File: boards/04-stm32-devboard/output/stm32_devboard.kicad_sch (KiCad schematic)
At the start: 17 parts, among them J1 SWD-6, U1 AMS1117-3.3, U2 STM32F103C8T6, Y1 8MHz

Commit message: chore(boards): regenerate schematics after crystal-factory refactor
Regenerates board 03/04/05 schematics from their refactored generator
scripts after rebase onto current main (post-merge of #2575/#2577/#2576).
Diff for board 03 shows two new C symbols (C5, C6 - the
previously-missing 22pF load caps); diffs for boards 04 and 05 are
mostly UUID changes since the refactor produces equivalent layouts.

Refs #2568.

Co-Authored-By: Claude Opus 4.7 (1M context) <noreply@anthropic.com>
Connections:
- net +5V: now also R2.1; no longer R2.2
- net at U2.26 (PB13): now also R2.2; no longer R2.1
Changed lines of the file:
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@@
 		(instances
 			(project "project"
-				(path "/44e716c7-27f0-4b1c-9394-2988dc26182d" (reference "U1") (unit 1)
+				(path "/d46a8a86-8bb3-4cd7-bb33-5e0ed20b6923" (reference "U1") (unit 1)
 				)
 			)
@@
 		(instances
 			(project "project"
-				(path "/44e716c7-27f0-4b1c-9394-2988dc26182d" (reference "C1") (unit 1)
+				(path "/d46a8a86-8bb3-4cd7-bb33-5e0ed20b6923" (reference "C1") (unit 1)
 				)
 			)
@@
 		(instances
 			(project "project"
-				(path "/44e716c7-27f0-4b1c-9394-2988dc26182d" (reference "C2") (unit 1)
+				(path "/d46a8a86-8bb3-4cd7-bb33-5e0ed20b6923" (reference "C2") (unit 1)
 				)
 			)
@@
 		(instances
 			(project "project"
-				(path "/44e716c7-27f0-4b1c-9394-2988dc26182d" (reference "C3") (unit 1)
+				(path "/d46a8a86-8bb3-4cd7-bb33-5e0ed20b6923" (reference "C3") (unit 1)
 				)
 			)
@@
 		(instances
 			(project "project"
-				(path "/44e716c7-27f0-4b1c-9394-2988dc26182d" (reference "U2") (unit 1)
+				(path "/d46a8a86-8bb3-4cd7-bb33-5e0ed20b6923" (reference "U2") (unit 1)
 				)
 			)
@@
 		(instances
 			(project "project"
-				(path "/44e716c7-27f0-4b1c-9394-2988dc26182d" (reference "C12") (unit 1)
+				(path "/d46a8a86-8bb3-4cd7-bb33-5e0ed20b6923" (reference "C12") (unit 1)
 				)
 			)
@@
 		(instances
 			(project "project"
-				(path "/44e716c7-27f0-4b1c-9394-2988dc26182d" (reference "C13") (unit 1)
+				(path "/d46a8a86-8bb3-4cd7-bb33-5e0ed20b6923" (reference "C13") (unit 1)
 				)
 			)
@@
 		(instances
 			(project "project"
-				(path "/44e716c7-27f0-4b1c-9394-2988dc26182d" (reference "C14") (unit 1)
+				(path "/d46a8a86-8bb3-4cd7-bb33-5e0ed20b6923" (reference "C14") (unit 1)
 				)
 			)
@@
 		(instances
 			(project "project"
-				(path "/44e716c7-27f0-4b1c-9394-2988dc26182d" (reference "C15") (unit 1)
+				(path "/d46a8a86-8bb3-4cd7-bb33-5e0ed20b6923" (reference "C15") (unit 1)
 				)
 			)
@@
 		(instances
 			(project "project"
-				(path "/44e716c7-27f0-4b1c-9394-2988dc26182d" (reference "C16") (unit 1)
+				(path "/d46a8a86-8bb3-4cd7-bb33-5e0ed20b6923" (reference "C16") (unit 1)
 				)
 			)
@@
 		(instances
 			(project "project"
-				(path "/44e716c7-27f0-4b1c-9394-2988dc26182d" (reference "Y1") (unit 1)
+				(path "/d46a8a86-8bb3-4cd7-bb33-5e0ed20b6923" (reference "Y1") (unit 1)
 				)
 			)
@@
 		(instances
 			(project "project"
-				(path "/44e716c7-27f0-4b1c-9394-2988dc26182d" (reference "C10") (unit 1)
+				(path "/d46a8a86-8bb3-4cd7-bb33-5e0ed20b6923" (reference "C10") (unit 1)
 				)
 			)
@@
 		(instances
 			(project "project"
-				(path "/44e716c7-27f0-4b1c-9394-2988dc26182d" (reference "C11") (unit 1)
+				(path "/d46a8a86-8bb3-4cd7-bb33-5e0ed20b6923" (reference "C11") (unit 1)
 				)
 			)
@@
 		(instances
 			(project "project"
-				(path "/44e716c7-27f0-4b1c-9394-2988dc26182d" (reference "J1") (unit 1)
+				(path "/d46a8a86-8bb3-4cd7-bb33-5e0ed20b6923" (reference "J1") (unit 1)
 				)
 			)
@@
 	(symbol
 		(lib_id "Device:R")
-		(at 171.45 147.32 270)
+		(at 171.45 152.4 0)
 		(unit 1)
 		(exclude_from_sim no)
@@
 		(dnp no)
 		(property "Reference" "R2"
-			(at 171.45 142.24 0)
+			(at 171.45 147.32 0)
 			(effects
 				(font
@@
 		)
 		(property "Value" "10k"
-			(at 171.45 144.78 0)
+			(at 171.45 149.86 0)
 			(effects
 				(font
@@
 		)
 		(property "Footprint" "Resistor_SMD:R_0805_2012Metric"
-			(at 171.45 147.32 0)
+			(at 171.45 152.4 0)
 			(effects
 				(font
@@
 		)
 		(property "Datasheet" "~"
-			(at 171.45 147.32 0)
+			(at 171.45 152.4 0)
 			(effects
 				(font
@@
 		(instances
 			(project "project"
-				(path "/44e716c7-27f0-4b1c-9394-2988dc26182d" (reference "R2") (unit 1)
+				(path "/d46a8a86-8bb3-4cd7-bb33-5e0ed20b6923" (reference "R2") (unit 1)
 				)
 			)
@@
 		(instances
 			(project "project"
-				(path "/44e716c7-27f0-4b1c-9394-2988dc26182d" (reference "D1") (unit 1)
+				(path "/d46a8a86-8bb3-4cd7-bb33-5e0ed20b6923" (reference "D1") (unit 1)
 				)
 			)
@@
 		(instances
 			(project "project"
-				(path "/44e716c7-27f0-4b1c-9394-2988dc26182d" (reference "R1") (unit 1)
+				(path "/d46a8a86-8bb3-4cd7-bb33-5e0ed20b6923" (reference "R1") (unit 1)
 				)
 			)
@@
 		(instances
 			(project "project"
-				(path "/44e716c7-27f0-4b1c-9394-2988dc26182d" (reference "#PWR01") (unit 1)
+				(path "/d46a8a86-8bb3-4cd7-bb33-5e0ed20b6923" (reference "#PWR01") (unit 1)
 				)
 			)
@@
 		(instances
 			(project "project"
-				(path "/44e716c7-27f0-4b1c-9394-2988dc26182d" (reference "#PWR02") (unit 1)
+				(path "/d46a8a86-8bb3-4cd7-bb33-5e0ed20b6923" (reference "#PWR02") (unit 1)
 				)
 			)
@@
 		(instances
 			(project "project"
-				(path "/44e716c7-27f0-4b1c-9394-2988dc26182d" (reference "#PWR03") (unit 1)
+				(path "/d46a8a86-8bb3-4cd7-bb33-5e0ed20b6923" (reference "#PWR03") (unit 1)
 				)
 			)
@@
 	)
 	(wire
-		(pts (xy 191.77 147.32) (xy 175.26 147.32))
-		(stroke
-			(width 0)
-			(type default)
-		)
-	)
-	(wire
-		(pts (xy 167.64 147.32) (xy 167.64 199.39))
+		(pts (xy 191.77 147.32) (xy 171.45 156.21))
+		(stroke
+			(width 0)
+			(type default)
+		)
+	)
+	(wire
+		(pts (xy 171.45 148.59) (xy 171.45 199.39))
 		(stroke
 			(width 0)
@@
 	)
 	(junction
-		(at 167.64 199.39)
+		(at 171.45 199.39)
 		(diameter 0)
 	)
@@
 	)
 	(sheet_instances
-		(path "/44e716c7-27f0-4b1c-9394-2988dc26182d" (page 1)
-		)
-	)
+		(path "/d46a8a86-8bb3-4cd7-bb33-5e0ed20b6923" (page 1)
+		)
+	)

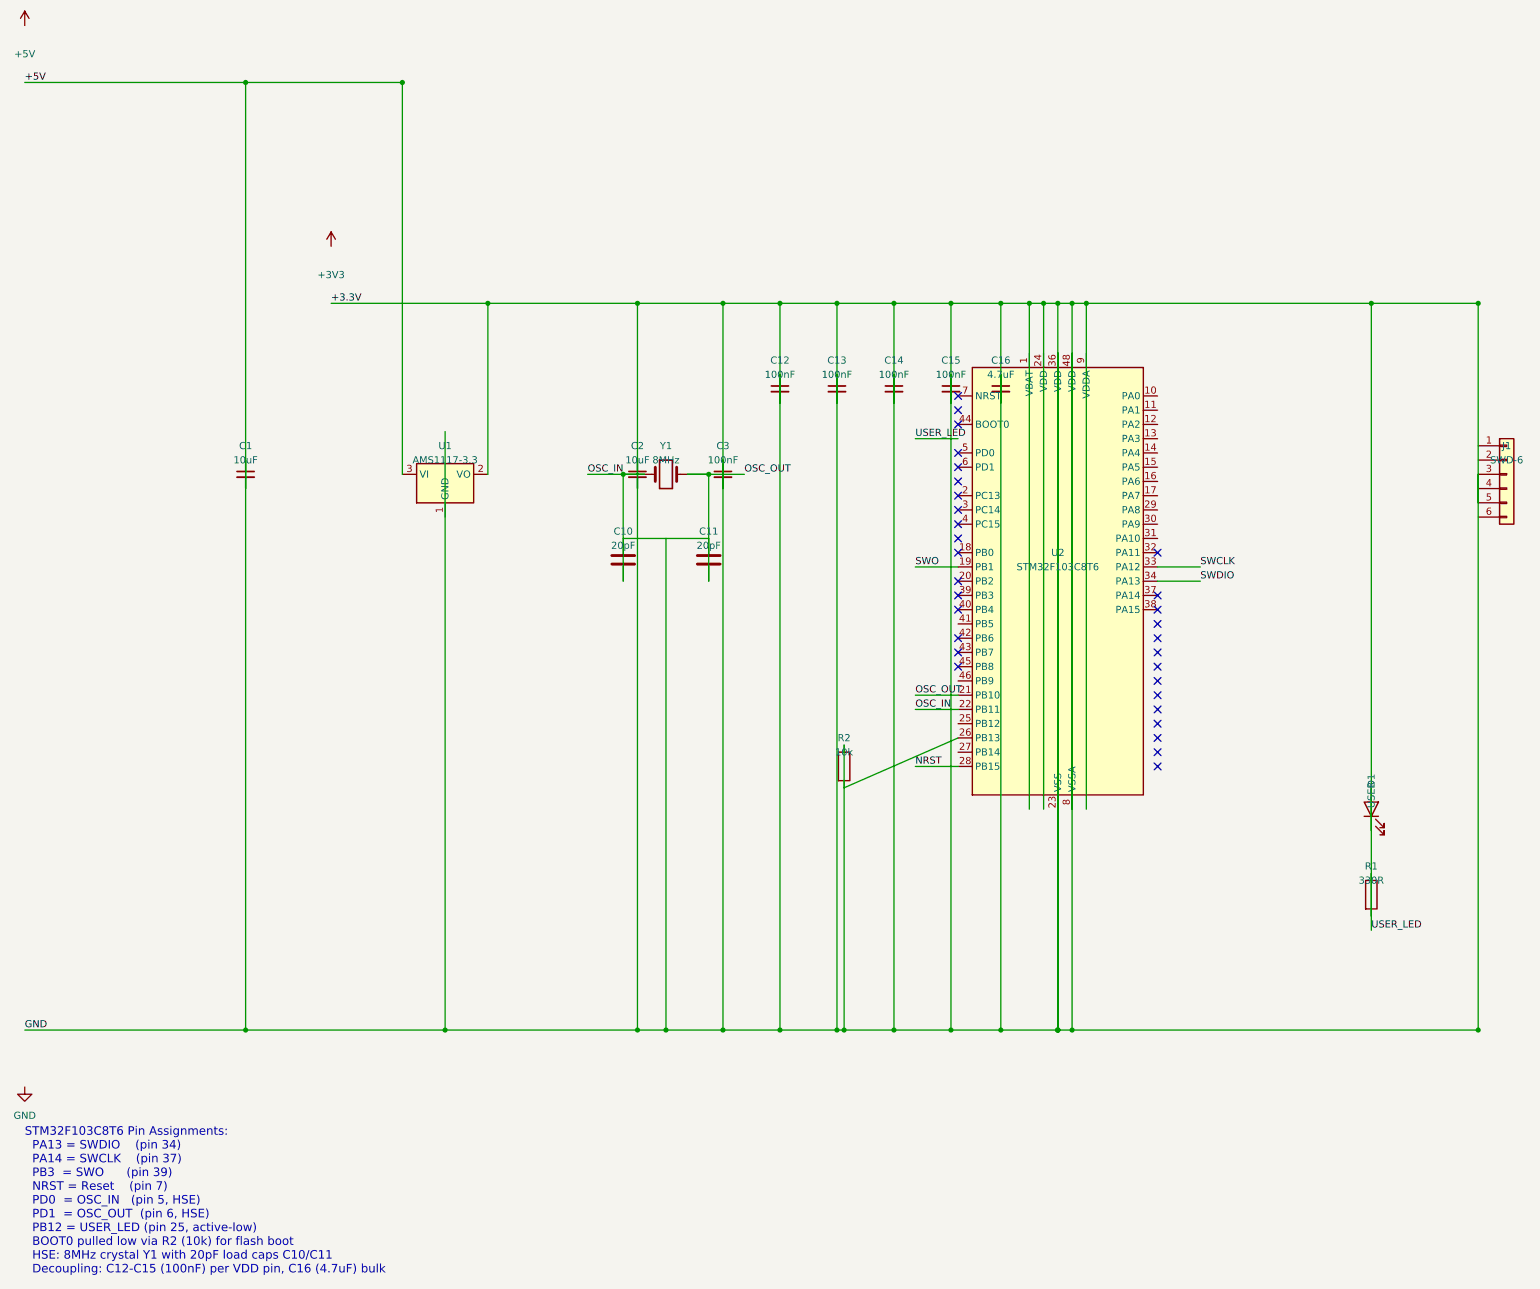
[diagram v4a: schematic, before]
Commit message: fix(board-04): bake --auto-mfr-tier into design.py route step (closes #2988) (#2997)
* fix(board-04): bake --auto-mfr-tier into design.py route step (closes #2988)

Adds --auto-mfr-tier to boards/04-stm32-devboard/generate_design.py's
route_pcb() subprocess invocation, matching the empirically-verified
recipe from PR #2982 (closes #2974) that achieved 9/9 signal nets
across 5/5 runs (3 default seeds + seed 1 + seed 42).

Before this change the in-script recipe was missing --auto-mfr-tier;
the default fleet recipe consistently regressed to 8/9 (NRST blocked
on the LQFP-48 west edge) even though the committed routed PCB on
main is from PR #2957's era when the recipe was 9/9-capable. This is
a "design.py output drifts from committed output" parity bug,
identical in shape to what PR #2981 fixed for board 05 (#2975).

Additionally, --mfr jlcpcb-tier1 is added to the kct stitch
invocation so the GND stitching vias use tier-1-compliant
dimensions (0.6mm diameter / 0.3mm drill). Without this, kct
stitch's default 0.45mm/0.2mm via tier-3 dimensions would cause
the post-stitch DRC to surface ~48 dimension_via_* errors against
jlcpcb-tier1 -- bypassing every previously-acceptable DRC outcome
on the regenerated artifact. The previous committed PCB on main was
in an unstitched state (3 vias total, all tier-1) due to historic
script ordering; the new committed PCB is fully stitched (25 vias).

Empirical outcome on the regenerated artifact:

- Net completion: 9/9 signal nets (NRST routed; 11/12 with GND
  plane stitched: U2.8 LQFP corner pad still skips, see #2842).
- DRC errors: 5 under jlcpcb-tier1 (3 clearance_segment_via +
  2 clearance_pad_via). All in the OSC_IN/OSC_OUT/SWO LQFP in-pad
  rescue cluster documented in the existing tolerance comment.

NOTE: The 5-error result is 1 over the current 4-error allowlist
floor for board 04. The 5th error is the SWO in-pad rescue (same
class as the existing 4); it fires consistently with the full
recipe because the recipe routes more 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
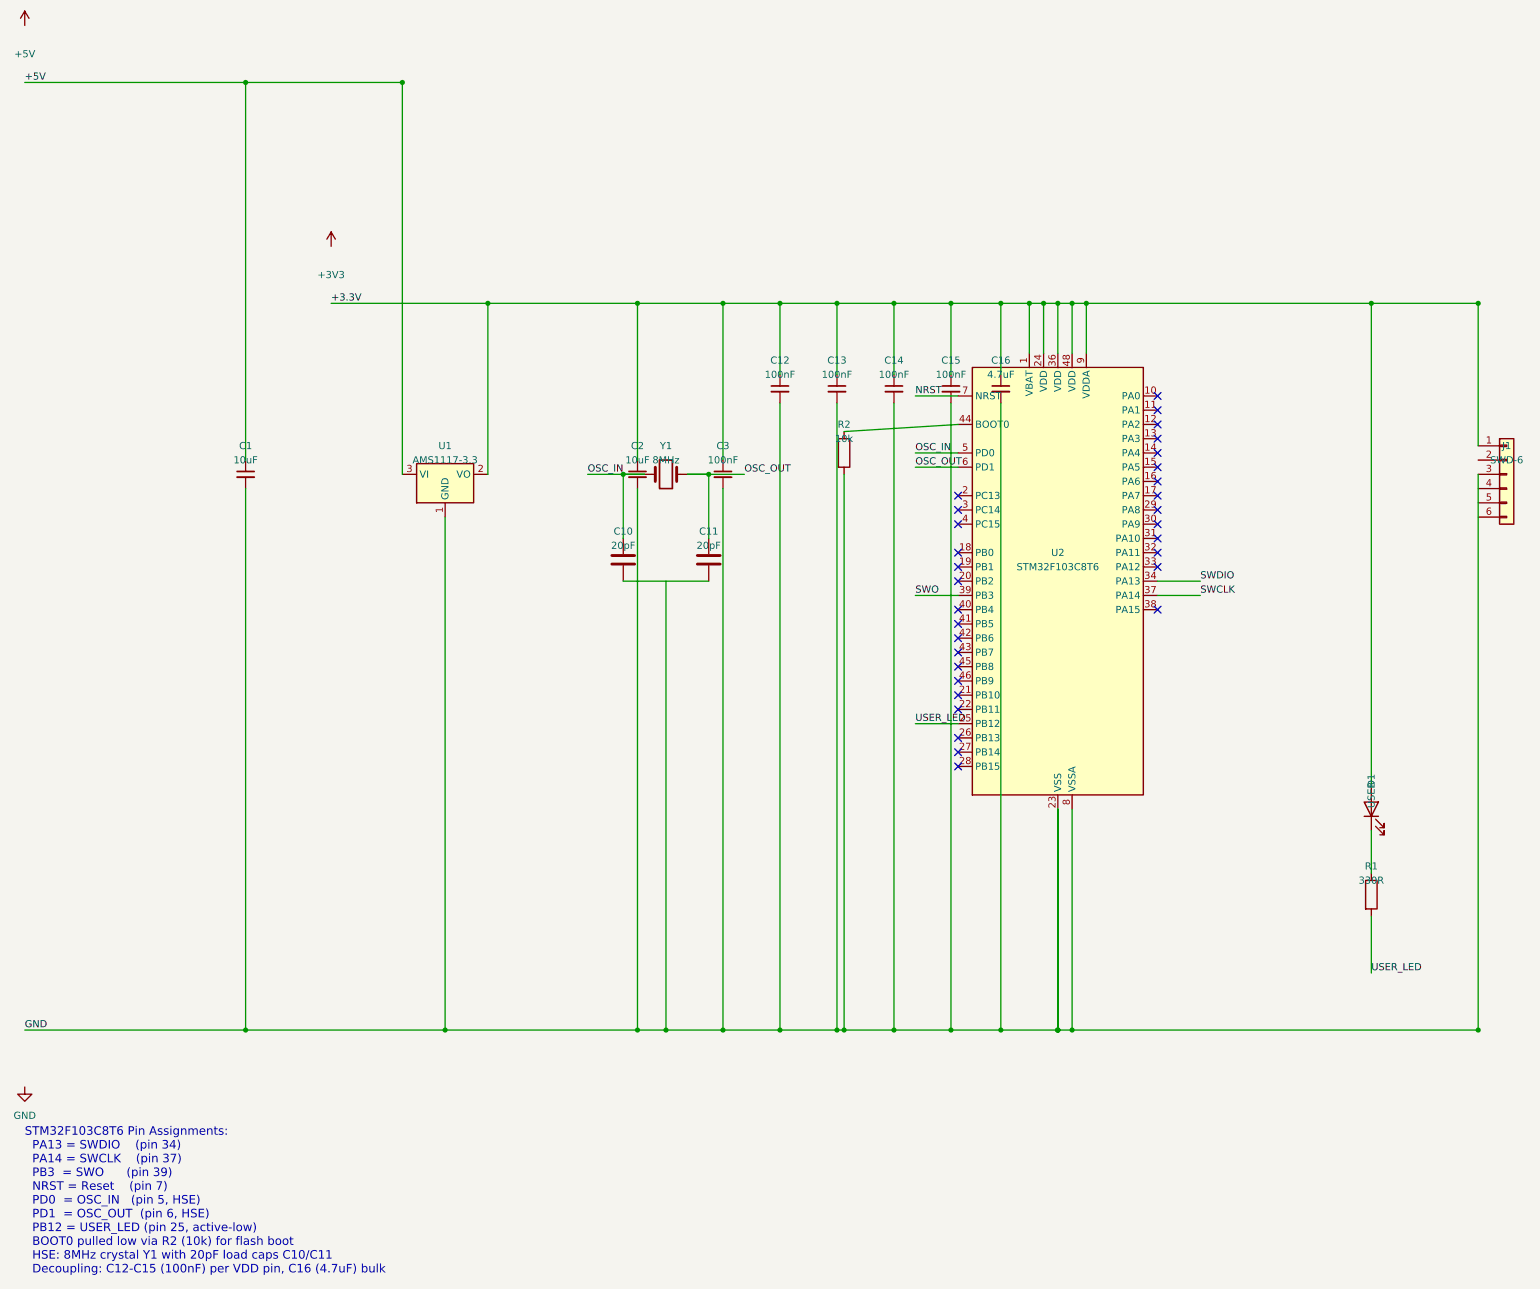
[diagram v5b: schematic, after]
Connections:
- net +5V: no longer C1.2, C12.1, C12.2, C13.1, C13.2, C14.1, C14.2, C15.1, C15.2, C16.1, C16.2, C2.1, C2.2, C3.1, C3.2, D1.1 (K), D1.2 (A), J1.3 (Pin_3), J1.5 (Pin_5), R1.1, R1.2, R2.1, U1.2 (VO), U2.23 (VSS), U2.35 (VSS), U2.36 (VDD), U2.47 (VSS), U2.48 (VDD), U2.8 (VSSA)
- net NRST: now also U2.7 (NRST); no longer U2.28 (PB15)
- net OSC_IN: now also C10.1, U2.5 (PD0); no longer C10.2, U2.22 (PB11)
- net OSC_OUT: now also C11.1, U2.6 (PD1); no longer C11.2, U2.21 (PB10)
- net SWCLK: now also U2.37 (PA14); no longer U2.33 (PA12)
- net SWO: now also U2.39 (PB3); no longer U2.19 (PB1)
- net at U2.26 (PB13): no longer R2.2
- net +3.3V: now reaches U2.1 (VBAT)
- net +3.3V: now also C12.1, C13.1, C14.1, C15.1, C16.1, C2.1, C3.1, D1.2 (A), J1.1 (Pin_1), U1.2 (VO), U2.24 (VDD), U2.36 (VDD), U2.48 (VDD), U2.9 (VDDA)
- net USER_LED: now reaches U2.25 (PB12)
- net USER_LED: now also R1.2
- net at U2.44 (BOOT0): now also R2.1
- net GND: now reaches U1.1 (GND)
- net GND: now also C1.2, C12.2, C13.2, C14.2, C15.2, C16.2, C2.2, C3.2, J1.3 (Pin_3), R2.2, U2.23 (VSS), U2.35 (VSS), U2.47 (VSS), U2.8 (VSSA)
- new net: D1.1 (K), R1.1
- new net: C10.2, C11.2

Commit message: fix(board-04): ERC PASS (11 -> 0 errors) via power-rail bridging + SWD pin_nets (closes #3149)
Board 04 (STM32 devboard) had 11 long-standing KiCad ERC errors -- the
fleet-audit "0 -> 11" delta was a false regression (the M-C closure
narrative recorded an inaccurate "ERC: 0 PASS"; the board had exactly
these 11 errors since PR #3116). Two independent defects in
generate_design.py, both fixed by mirroring sister board 05's PR #3004:

Cluster A (6 errors): the three add_power() symbols (+5V, +3V3, GND) were
placed 10mm from their rails with no bridging wire, so each symbol pin
floated (pin_not_connected) and the undriven +5V/GND rails fired
power_pin_not_driven on U1.VI/U1.GND/#PWR02. Fixed by wiring each symbol
to its rail, adding a PWR_FLAG on +5V and GND (no power_output driver),
and renaming the 3.3V rail label "+3.3V" -> "+3V3" to unify with the
stock power:+3V3 symbol (avoids the synthesized-symbol lib_symbol_issues
warning).

Cluster B (5 issues): the SWD DebugHeader (J1) was created without
pin_nets, leaving pins 2/4/5/6 (SWDIO/SWCLK/GND-key/NRST) floating and the
MCU-side SWD labels isolated. Fixed by passing
pin_nets={"2":"SWDIO","4":"SWCLK","5":"GND","6":"NRST"}.

Also adds a junction at the crystal GND port to clear the
unconnected_wire_endpoint warning (the connect_to_rails vertical drop taps
the C10/C11 ground-bus mid-segment). The single residual warning
(isolated_pin_label on SWO) is design intent: PB3/SWO has no SWD-6 pin.

Verified end-to-end: ERC 0 errors, routing 9/9 signal nets, GND 17/18
pads stitched (U2.8 stranded is documented design intent per #3081).
Adds tests/test_board_04_erc_regression.py (modeled on board 05's) with
per-cluster assertions. The DebugHeader pin_nets path is already covered
by tests/test_blocks_debug_header.py.

Co-Authored-By: Claude Opus 4.7 (1M context) <noreply@anthropic.com>
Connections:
- net +3.3V is gone; now on net +3V3: C12.1, C13.1, C14.1, C15.1, C16.1, C2.1, C3.1, D1.2 (A), J1.1 (Pin_1), U1.2 (VO), U2.1 (VBAT), U2.24 (VDD), U2.36 (VDD), U2.48 (VDD), U2.9 (VDDA)
- net GND: now also C10.2, C11.2, J1.5 (Pin_5)
- net NRST: now also J1.6 (Pin_6)
- net SWCLK: now also J1.4 (Pin_4)
- net SWDIO: now also J1.2 (Pin_2)
